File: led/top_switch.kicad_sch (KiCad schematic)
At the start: 13 parts, among them IC2 LM2903P, Q12 IRF9540N, Q13 BS170, Q14 IRF9540N, Q8 BS170, Q9 BS170, U2 TLP240, U3 TLP240

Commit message: changed measurement resistor in current driver
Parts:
- R4: Manufacturer_Name Stackpole Electronics, Inc. -> (none); Manufacturer_Part_Number RSF1JT1R00 -> MF0207FRE52-1R; Mouser Part Number 708-RSF1JT1R00 -> 603-MF0207FRE52-1R
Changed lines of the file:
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@@
 			)
 		)
-		(property "Datasheet" "https://cs.seielect.com/catalog/SEI-RSF_RSMF.pdf"
+		(property "Datasheet" ""
 			(at 357.48 91.44 0)
 			(effects
@@
 			)
 		)
-		(property "Mouser Part Number" "708-RSF1JT1R00"
+		(property "Mouser Part Number" "603-MF0207FRE52-1R"
 			(at 657.48 91.44 0)
 			(effects
@@
 			)
 		)
-		(property "Manufacturer_Name" "Stackpole Electronics, Inc."
+		(property "Manufacturer_Name" ""
 			(at 857.48 91.44 0)
 			(effects
@@
 			)
 		)
-		(property "Manufacturer_Part_Number" "RSF1JT1R00"
+		(property "Manufacturer_Part_Number" "MF0207FRE52-1R"
 			(at 957.48 91.44 0)
 			(effects

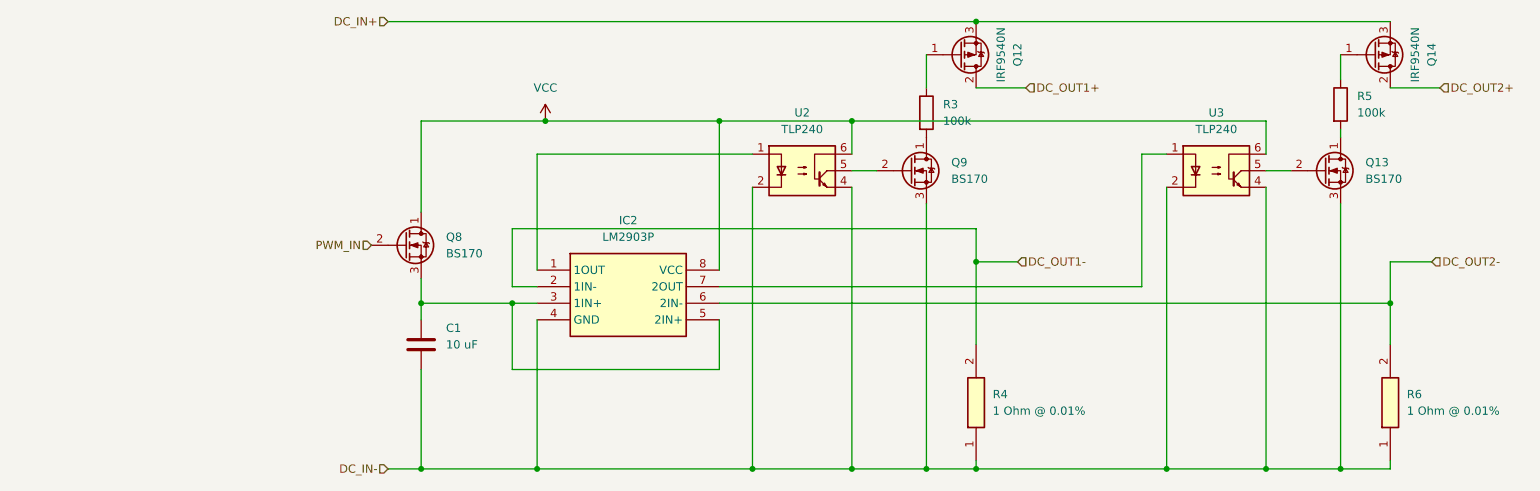
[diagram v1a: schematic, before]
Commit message: top switch, capacitor design doc
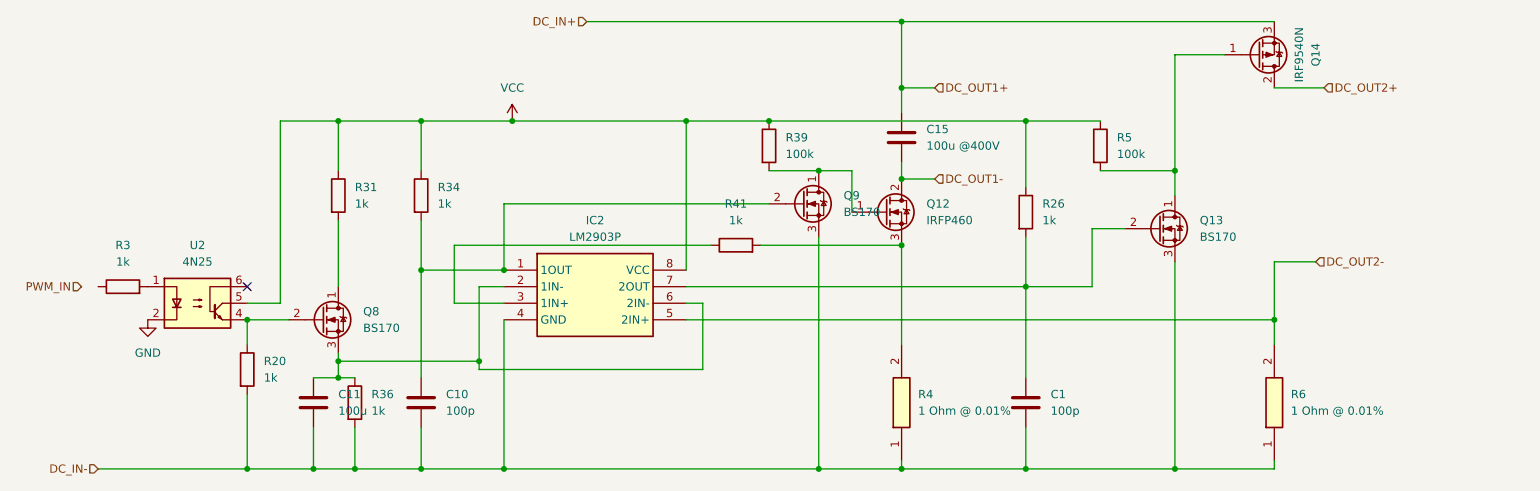
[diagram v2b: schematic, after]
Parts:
- removed Q12: IRF9540N, Package_TO_SOT_THT:TO-220-3_Vertical, symbol Transistor_FET:IRF9540N
- removed U3: TLP240, Package_DIP:DIP-4_W7.62mm, symbol Isolator:4N25
- added C10: 100p, Capacitor_THT:C_Disc_D8.0mm_W5.0mm_P10.00mm, symbol Device:C
- added C11: 100u, Capacitor_THT:C_Disc_D8.0mm_W5.0mm_P10.00mm, symbol Device:C
- added C15: 100u @400V, Capacitor_THT:C_Disc_D8.0mm_W5.0mm_P10.00mm, symbol Device:C
- added Q12: IRFP460, Package_TO_SOT_THT:TO-247-3_Vertical, symbol Transistor_FET:IRFP4468PbF
- added R20, R26, R31, R34, R36, R41: 1k, Resistor_THT:R_Axial_DIN0207_L6.3mm_D2.5mm_P2.54mm_Vertical, symbol Device:R
- added R39: 100k, Resistor_THT:R_Axial_DIN0204_L3.6mm_D1.6mm_P2.54mm_Vertical, symbol Device:R
- C1: value 10 uF -> 100p; footprint Resistor_THT:R_Axial_DIN0204_L3.6mm_D1.6mm_P2.54mm_Vertical -> Capacitor_THT:C_Disc_D8.0mm_W5.0mm_P10.00mm; Mouser Part Number 581-TAP106K025CRS -> 791-YP501101K40AND5
- R3: value 100k -> 1k; footprint Resistor_THT:R_Axial_DIN0204_L3.6mm_D1.6mm_P2.54mm_Vertical -> Resistor_THT:R_Axial_DIN0207_L6.3mm_D2.5mm_P2.54mm_Vertical; Mouser Part Number 603-MFR-25FTE52-100K -> 708-CF12JT1K00
- U2: value TLP240 -> 4N25; footprint Package_DIP:DIP-4_W7.62mm -> Package_DIP:DIP-6_W7.62mm; Mouser Part Number 757-TLP240AD4F -> (none)
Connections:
- net DC_IN+: now also C15.1
- net DC_IN-: now also C10.2, C11.1, R20.2, R36.2; no longer U2.2, U2.4
- net DC_OUT1-: now also C15.2, Q12.2 (D); no longer IC2.2 (1IN-), R4.2
- net DC_OUT2-: now also IC2.5 (2IN+); no longer IC2.6 (2IN-)
- net PWM_IN: no longer Q8.2 (G)
- net VCC: now also R5.1, U2.5, R26.1, R31.1, R34.1, R39.1; no longer Q8.1 (D), U2.6
- net at R3.2: now also U2.1; no longer Q9.1 (D)
- net at IC2.1 (1OUT): now also Q9.2 (G), C10.1, R34.2; no longer U2.1
- net at IC2.7 (2OUT): now also C1.1, Q13.2 (G), R26.2
- net at Q13.1 (D), R5.2: now also Q14.1 (G)
- new net: Q12.3 (S), R4.2, R41.2
- new net: C11.2, IC2.2 (1IN-), IC2.6 (2IN-), Q8.3 (S), R36.1
- new net: Q12.1 (G), Q9.1 (D), R39.2
- new net: IC2.3 (1IN+), R41.1
- new net: Q8.2 (G), R20.1, U2.4
- new net: Q8.1 (D), R31.2
- new net GND: U2.2
- no-connect marks 0 -> 1
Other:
- moved on the sheet: IC2, Q13, Q14, Q9, R4, R5, R6
